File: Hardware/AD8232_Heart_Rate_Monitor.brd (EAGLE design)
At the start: 1 part

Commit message: Initial board design
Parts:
- added C1: 1nF, SparkFun-Passives:0603-CAP
- added C2: .1uf, SparkFun-Passives:0603-CAP
- added C3: .1uF, SparkFun-Passives:0603-CAP
- added C4, C5: 0.33uF, SparkFun-Passives:0603-CAP
- added C6: 1.5nF, SparkFun-Passives:0603-CAP
- added C7: 10nF, SparkFun-Passives:0603-CAP
- added JP1: (no value), SparkFun-Connectors:1X05
- added LOGO1: SFE_LOGO_NAME_FLAME.1_INCH, SparkFun-Aesthetics:SFE_LOGO_NAME_FLAME_.1
- added LOGO2: OSHW-LOGOM, SparkFun-Aesthetics:OSHW-LOGO-M
- added R1, R2: 180k, SparkFun-Passives:0603-RES
- added R10, R11: 1.4M, SparkFun-Passives:0603-RES
- added R12, R4, R5, R8, R9: 10M, SparkFun-Passives:0603-RES
- added R13, R3, R6: 1M, SparkFun-Passives:0603-RES
- added R14: 360k, SparkFun-Passives:0603-RES
- added R7: 100k, SparkFun-Passives:0603-RES
- added SJ1, SJ2: (no value), SparkFun-Passives:SJ_3_PASTE1&2
- added STANDOFF1, STANDOFF2, STANDOFF3, STANDOFF4: STAND-OFF, SparkFun-Electromechanical:STAND-OFF
- added U1: AD8232, AD8232:LFCSP_20
- added U2: (no value), SparkFun-Connectors:AUDIO-JACK-3.5MM-SMD
- moved FRAME1 14.5 mm to (0.00, -8.89)
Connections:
- new net 3.3V: C3.1, JP1.2, R5.1, SJ1.1, SJ2.3, U1.15, U1.17
- new net GND: C2.2, C3.2, JP1.1, R12.1, SJ2.1, U1.16, U1.PAD
- new net LA: R1.1, R9.1, U2.RING
- new net LO+: JP1.4, U1.12
- new net LO-: JP1.3, U1.11
- new net N$1: R1.2, U1.2
- new net N$13: C5.1, U1.1
- new net N$14: R10.1, R11.2, R4.2
- new net N$16: C4.1, R10.2, SJ1.3, U1.6
- new net N$17: C1.1, U1.4
- new net N$18: C1.2, R14.1, U1.5
- new net N$2: R2.2, U1.3
- new net N$20: R8.2, R9.2, SJ1.2
- new net N$21: SJ2.2, U1.14
- new net N$3: C7.2, R3.2, U1.7
- new net N$4: C5.2, R4.1, U1.20
- new net N$5: C2.1, R12.2, R5.2, U1.18
- new net N$7: R6.2, R7.1, U1.9
- new net N$8: R11.1, R13.2, U1.19
- new net N$9: C6.2, R13.1, R3.1
- new net RA: R2.1, R8.1, U2.SLEEVE
- new net REFOUT: C4.2, C7.1, R7.2, U1.8
- new net RL: R14.2, U2.TIP
- new net SDN: JP1.5, U1.13
- new net SIGNAL_OUT: C6.1, R6.1, U1.10
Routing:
- net 3.3V: track 0.00 -> 45.9 mm, vias 0 -> 3
- net N$8: track 0.00 -> 26.5 mm, vias 0 -> 3
- net LO-: track 0.00 -> 25.1 mm
- net LO+: track 0.00 -> 23.4 mm
- net SDN: track 0.00 -> 22.2 mm
- net REFOUT: track 0.00 -> 19.8 mm, vias 0 -> 2
- net N$16: track 0.00 -> 19.0 mm, vias 0 -> 2
- net N$20: track 0.00 -> 18.7 mm, vias 0 -> 2
- net RA: track 0.00 -> 15.6 mm
- net RL: track 0.00 -> 10.7 mm
- net SIGNAL_OUT: track 0.00 -> 9.93 mm
- net LA: track 0.00 -> 7.60 mm
- net N$18: track 0.00 -> 6.85 mm
- net N$7: track 0.00 -> 5.71 mm
- net N$21: track 0.00 -> 5.43 mm
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- added copper zone on layer 1, net 3.3V
- added copper zone on layer 1, net GND
- added copper zone on layer 16, net GND
- added copper zone on layer 1, net N$14
- added copper zone on layer 1, net N$16
- added copper zone on layer 1, net N$3
- added copper zone on layer 1, net N$4
- added copper zone on layer 1, net N$5
- added copper zone on layer 1, net N$9
- added copper zone on layer 1, net REFOUT
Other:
- board outline added: 35.6 x 27.9 mm
- board text added: "!SDN"
- board text added: "3.3v"
- board text added: "GND"
- board text added: "LO+"
- board text added: "LO-"

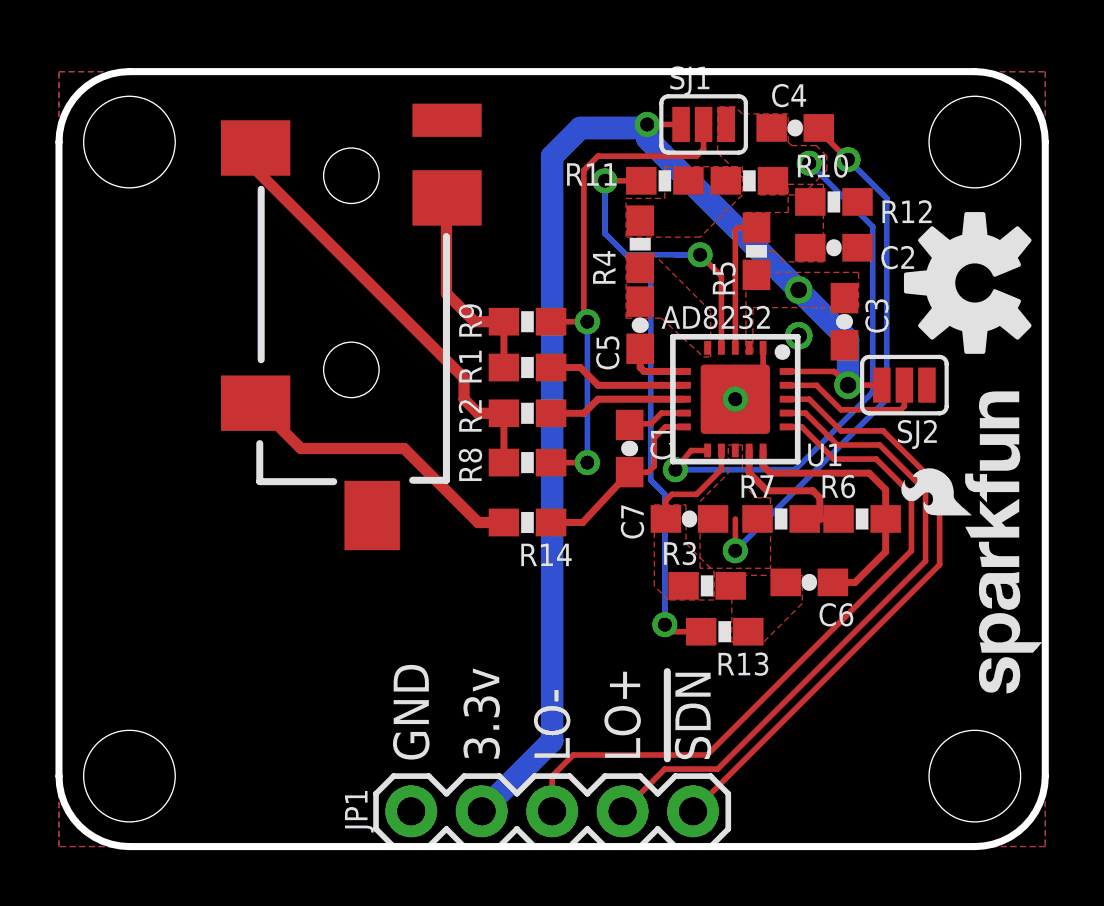
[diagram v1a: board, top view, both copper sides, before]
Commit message: Fixed silk and updated capacitors to appropriate sizes.
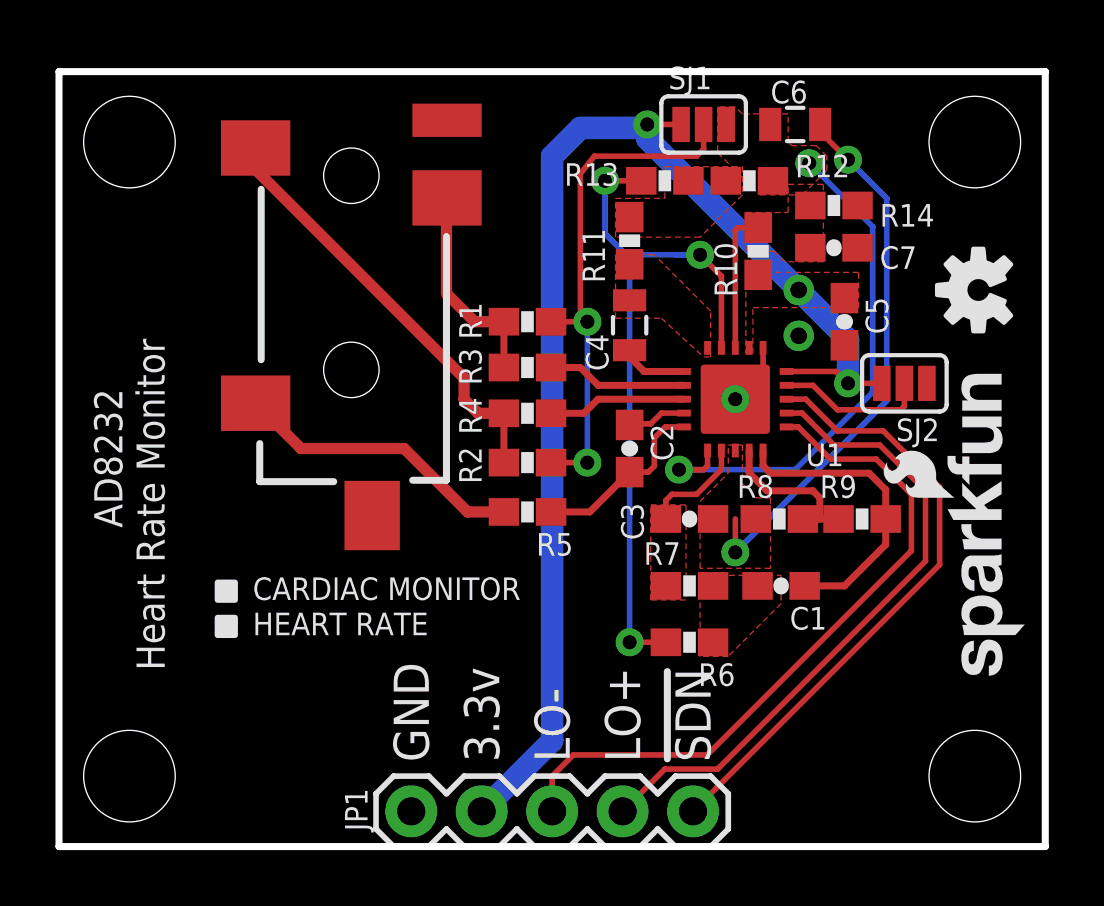
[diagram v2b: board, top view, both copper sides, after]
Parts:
- C1: value 1nF -> 1.5nF
- C2: value .1uf -> 1nF
- C3: value .1uF -> 10nF
- C4: device SparkFun-Passives:0603-CAP -> SparkFun-Capacitors:0805
- C5: value 0.33uF -> .1uF
- C6: value 1.5nF -> 0.33uF; device SparkFun-Passives:0603-CAP -> SparkFun-Capacitors:0805
- C7: value 10nF -> .1uf
- LOGO1: value SFE_LOGO_NAME_FLAME.1_INCH -> OSHW-LOGOS; device SparkFun-Aesthetics:SFE_LOGO_NAME_FLAME_.1 -> SparkFun-Aesthetics:OSHW-LOGO-S
- LOGO2: value OSHW-LOGOM -> SFE_LOGO_NAME_FLAME.1_INCH; device SparkFun-Aesthetics:OSHW-LOGO-M -> SparkFun-Aesthetics:SFE_LOGO_NAME_FLAME_.1
- R1, R2: value 180k -> 10M
- R10, R11: value 1.4M -> 10M
- R12: value 10M -> 1.4M
- R13: value 1M -> 1.4M
- R14: value 360k -> 10M
- R3: value 1M -> 180k
- R4: value 10M -> 180k
- R5: value 10M -> 360k
- R7: value 100k -> 1M
- R8: value 10M -> 100k
- R9: value 10M -> 1M
- moved STANDOFF3 38.1 mm to (33.0, 2.54)
- moved STANDOFF4 38.1 mm to (2.54, 2.54)
- moved STANDOFF1 22.9 mm to (2.54, 25.4)
- moved STANDOFF2 22.9 mm to (33.0, 25.4)
- moved C6 16.5 mm to (26.5, 26.0), turned to 0 degrees
- moved R13 16.4 mm to (21.8, 24.0), turned to 0 degrees
- moved R14 15.9 mm to (27.9, 23.1)
- moved LOGO1 15.2 mm to (33.1, 20.1)
- moved LOGO2 14.7 mm to (34.9, 5.71)
- moved R9 14.0 mm to (29.0, 11.8), turned to 180 degrees
- moved R5 12.5 mm to (16.9, 12.1), turned to 180 degrees
- moved C7 11.1 mm to (27.9, 21.6), turned to 0 degrees
- moved C2 10.3 mm to (20.6, 14.4), turned to 270 degrees
- moved R3 10.2 mm to (16.9, 17.3), turned to 0 degrees
- moved R8 9.31 mm to (26.0, 11.8), turned to 180 degrees
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- renumbered U2 to JP2
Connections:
- net 3.3V: now also C5.1, R10.1; no longer C3.1, R5.1
- net GND: now also C5.2, C7.2, R14.1; no longer C2.2, C3.2, R12.1
- net LA: now also R3.1; no longer R9.1
- net N$1: now also R3.2; no longer R1.2
- net N$13: now also C4.1; no longer C5.1
- net N$14: now also R12.1, R13.2; no longer R10.1, R4.2
- net N$16: now also C6.1, R12.2; no longer C4.1, R10.2
- net N$17: now also C2.1; no longer C1.1
- net N$18: now also C2.2, R5.1; no longer C1.2, R14.1
- net N$2: now also R4.2; no longer R2.2
- net N$20: now also R1.2, R2.2; no longer R8.2, R9.2
- net N$3: now also C3.2, R7.2; no longer C7.2, R3.2
- net N$4: now also C4.2, R11.1; no longer C5.2, R4.1
- net N$5: now also C7.1, R10.2, R14.2; no longer C2.1, R12.2, R5.2
- net N$7: now also R8.1, R9.2; no longer R6.2, R7.1
- net N$8: now also R13.1, R6.2; no longer R11.1, R13.2
- net N$9: now also C1.2, R6.1, R7.1; no longer C6.2, R13.1, R3.1
- net RA: now also R4.1; no longer R8.1
- net REFOUT: now also C3.1, C6.2, R8.2; no longer C4.2, C7.1, R7.2
- net RL: now also R5.2; no longer R14.2
- net SIGNAL_OUT: now also C1.1, R9.1; no longer C6.1, R6.1
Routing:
- net SIGNAL_OUT: track 9.93 -> 10.8 mm
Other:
- outline, holes or cut-outs redrawn
- board text added: "AD8232"
- board text added: "CARDIAC MONITOR"
- board text added: "HEART RATE"
- board text added: "Heart Rate Monitor"

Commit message: Fixed cap values
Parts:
- C5: value .1uF -> 0.1uF
- C7: value .1uf -> 0.1uf
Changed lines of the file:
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@@
 <attribute name="VALUE" x="19.431" y="15.367" size="0.4064" layer="27" font="vector" rot="R270"/>
 </element>
-<element name="C7" library="SparkFun-Passives" package="0603-CAP" value=".1uf" x="27.94" y="21.59" smashed="yes">
+<element name="C7" library="SparkFun-Passives" package="0603-CAP" value="0.1uf" x="27.94" y="21.59" smashed="yes">
 <attribute name="NAME" x="29.591" y="20.828" size="0.8128" layer="25" font="vector" ratio="15"/>
 <attribute name="VALUE" x="26.924" y="20.447" size="0.4064" layer="27" font="vector"/>
 </element>
-<element name="C5" library="SparkFun-Passives" package="0603-CAP" value=".1uF" x="28.321" y="18.923" smashed="yes" rot="R270">
+<element name="C5" library="SparkFun-Passives" package="0603-CAP" value="0.1uF" x="28.321" y="18.923" smashed="yes" rot="R270">
 <attribute name="NAME" x="29.083" y="19.812" size="0.8128" layer="25" font="vector" ratio="15" rot="R270"/>
 <attribute name="VALUE" x="27.178" y="19.939" size="0.4064" layer="27" font="vector" rot="R270"/>
